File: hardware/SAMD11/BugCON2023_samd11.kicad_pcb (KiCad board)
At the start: 2 copper layers, 47.9 x 38.3 mm, 26 parts, among them J1 Conn_01x04_Pin, J2 Conn_01x04_Pin, P1 USB_C_Plug_USB2.0, Q1 DMG3415U-7, SW1 SW_Push, SW2 ON, U1 ATSAMD11C14A-SS, U2 AP2112K-3.3

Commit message: add pins of usb on samd11
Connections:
- U1 pad 10: unconnected-(U1-PA25-Pad10) -> /D+
- U1 pad 9: unconnected-(U1-PA24-Pad9) -> /D-
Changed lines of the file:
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@@
   (net 28 "unconnected-(U1-PA08{slash}XIN-Pad2)")
   (net 29 "unconnected-(U1-PA09{slash}XOUT-Pad3)")
-  (net 30 "unconnected-(U1-PA24-Pad9)")
-  (net 31 "unconnected-(U1-PA25-Pad10)")
-  (net 32 "unconnected-(U1-PA04-Pad14)")
+  (net 30 "unconnected-(U1-PA04-Pad14)")
   (footprint "BugCON2023_samd11:bug_silk_5" (layer "F.Cu")
     (at 166.61 95.66)
@@
       (net 21 "/SWDIO") (pinfunction "PA31/SWDIO") (pintype "bidirectional"))
     (pad "9" smd roundrect (at 2.475 -2.54 270) (size 1.95 0.6) (layers "B.Cu" "B.Paste" "B.Mask") (roundrect_rratio 0.25)
-      (net 30 "unconnected-(U1-PA24-Pad9)") (pinfunction "PA24") (pintype "bidirectional+no_connect"))
+      (net 15 "/D-") (pinfunction "PA24") (pintype "bidirectional"))
     (pad "10" smd roundrect (at 2.475 -1.27 270) (size 1.95 0.6) (layers "B.Cu" "B.Paste" "B.Mask") (roundrect_rratio 0.25)
-      (net 31 "unconnected-(U1-PA25-Pad10)") (pinfunction "PA25") (pintype "bidirectional+no_connect"))
+      (net 14 "/D+") (pinfunction "PA25") (pintype "bidirectional"))
     (pad "11" smd roundrect (at 2.475 0 270) (size 1.95 0.6) (layers "B.Cu" "B.Paste" "B.Mask") (roundrect_rratio 0.25)
       (net 2 "GND") (pinfunction "GND") (pintype "power_in"))
@@
       (net 22 "unconnected-(U1-PA02-Pad13)") (pinfunction "PA02") (pintype "bidirectional+no_connect"))
     (pad "14" smd roundrect (at 2.475 3.81 270) (size 1.95 0.6) (layers "B.Cu" "B.Paste" "B.Mask") (roundrect_rratio 0.25)
-      (net 32 "unconnected-(U1-PA04-Pad14)") (pinfunction "PA04") (pintype "bidirectional+no_connect"))
+      (net 30 "unconnected-(U1-PA04-Pad14)") (pinfunction "PA04") (pintype "bidirectional+no_connect"))
     (model "${KICAD6_3DMODEL_DIR}/Package_SO.3dshapes/SOIC-14_3.9x8.7mm_P1.27mm.wrl"
       (offset (xyz 0 0 0))

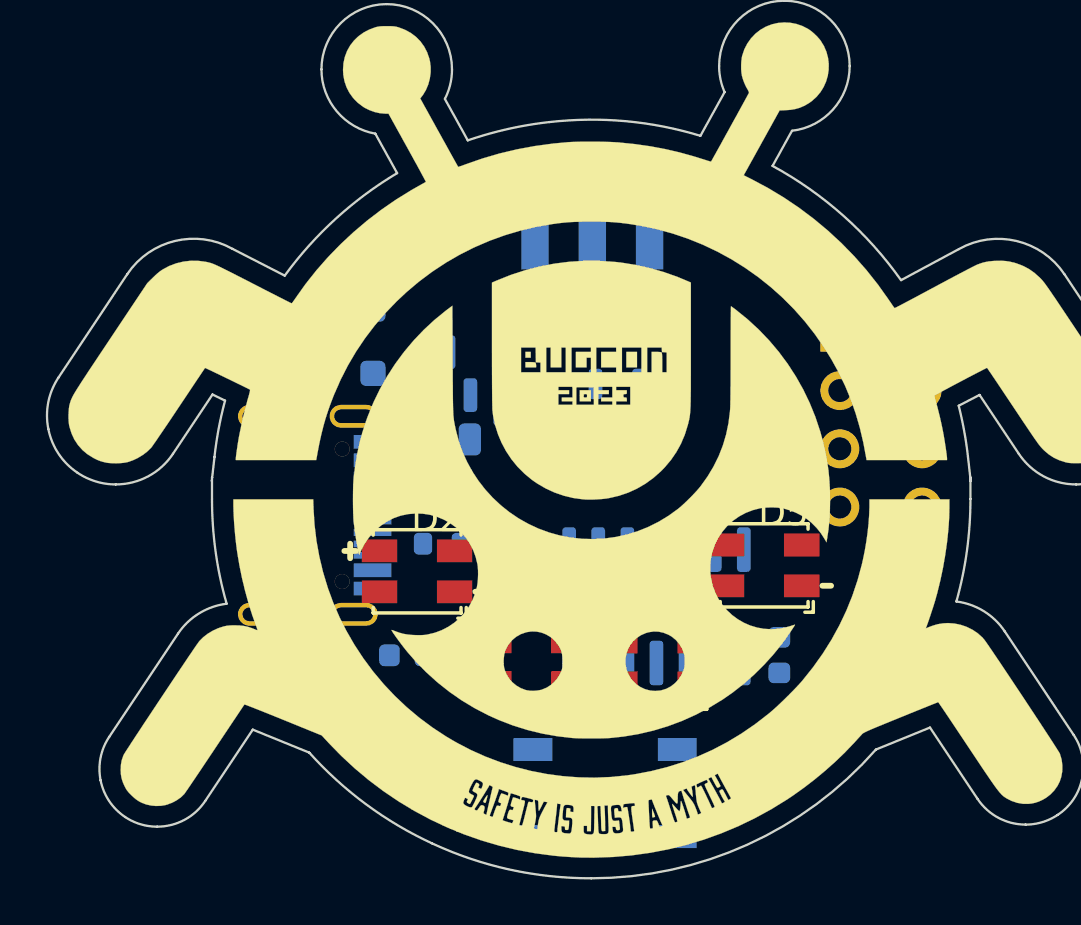
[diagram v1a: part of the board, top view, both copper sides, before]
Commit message: add floorplan to samd11
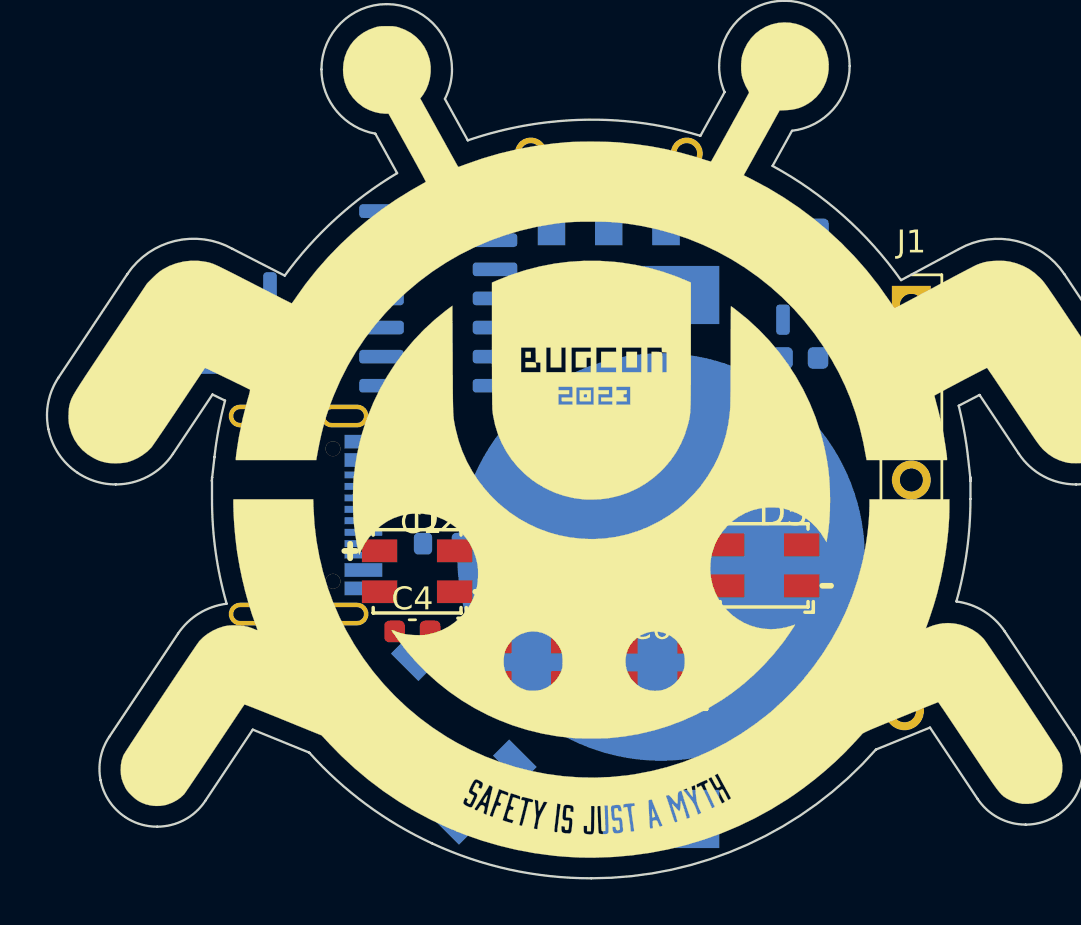
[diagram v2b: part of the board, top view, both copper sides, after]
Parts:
- added BT1: Battery_Cell, BugCON2023_samd11:BATHLD001THM, B.Cu at (143.2, 70.3)
- C1, C4, C6, C7, J1: moved to F.Cu
- moved U1 16.5 mm to (133.5, 59.1), turned to 180 degrees
- moved C1 13.6 mm to (132.7, 67.4), turned to 180 degrees
- moved R2 12.8 mm to (121.9, 62.2), turned to -90 degrees
- moved F1 11.2 mm to (123.6, 60.9), turned to 90 degrees
- moved R3 11.0 mm to (126.2, 62.4), turned to 180 degrees
- moved D1 11.0 mm to (119.9, 63.3)
- moved R4 10.6 mm to (138.4, 59.5), turned to -90 degrees
- moved C5 9.76 mm to (127.3, 75.5)
- moved J2 8.92 mm to (153.8, 69.4)
- moved C2 8.65 mm to (149.3, 56.0)
- moved U2 8.65 mm to (149.5, 58.9)
- moved C3 8.65 mm to (149.3, 61.7)
- moved Q1 8.26 mm to (126.1, 59.6)
- moved SW1 7.85 mm to (133.2, 78.4), turned to -45 degrees
- moved C6 6.18 mm to (142.7, 72.0), turned to 180 degrees
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
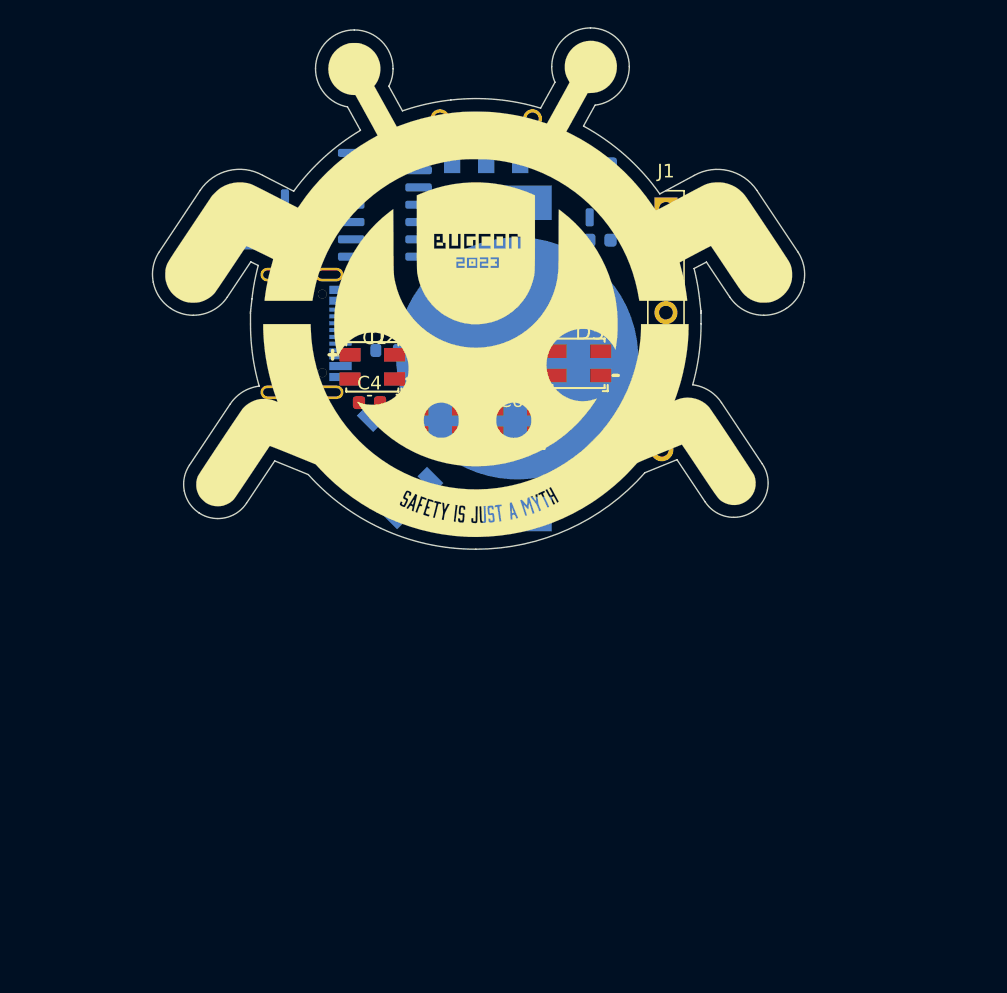
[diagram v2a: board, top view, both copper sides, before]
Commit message: upd floorplan on samd11
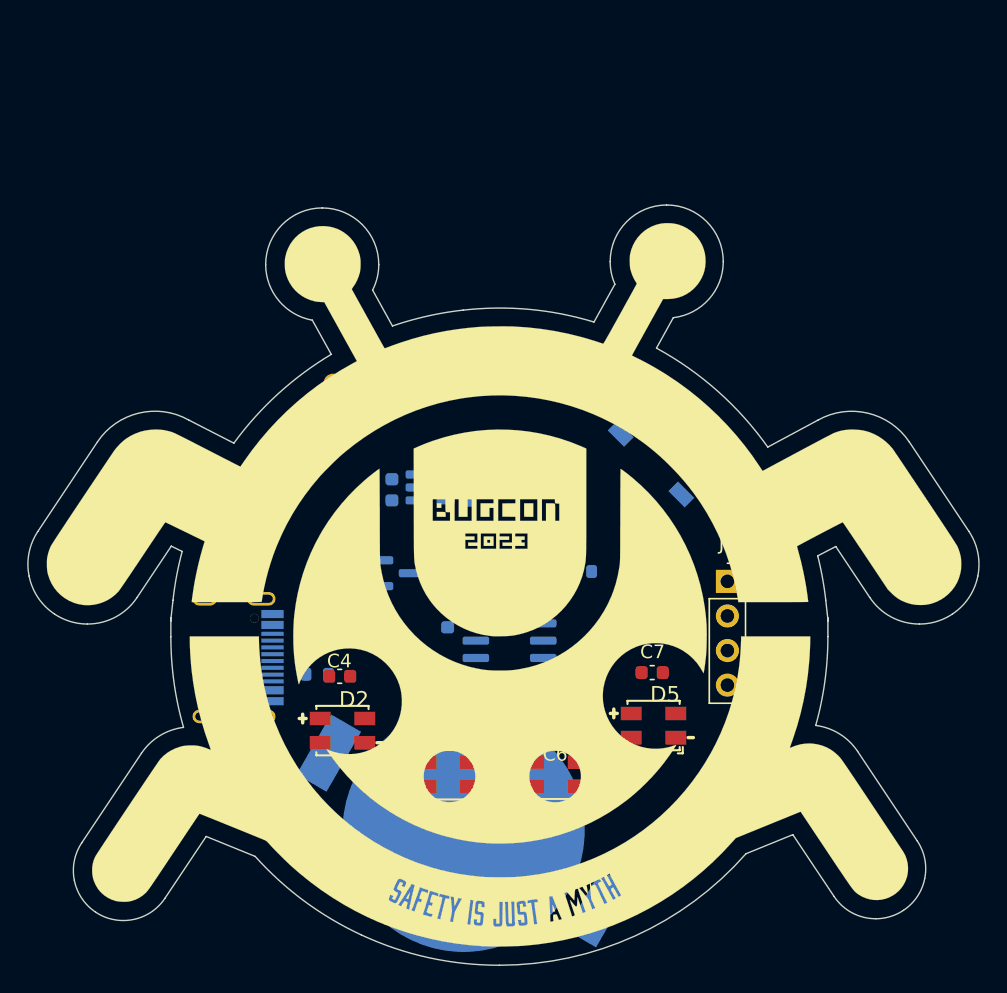
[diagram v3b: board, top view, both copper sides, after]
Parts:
- removed the Ref** at (166.6, 95.7)
- added ?: , , F.Cu at (141.8, 75.2)
- added Ref**: Val**, BugCON2023_samd11:bug-Silk_7, F.Cu at (142.2, 87.0)
- C1: moved to B.Cu
- C5: moved to F.Cu
- moved BT1 34.9 mm to (139.2, 105.0), turned to 150 degrees
- moved U1 32.1 mm to (142.6, 89.8)
- moved R2 29.2 mm to (128.6, 90.6), turned to 180 degrees
- moved F1 28.5 mm to (128.8, 88.9), turned to 0 degrees
- moved C2 28.4 mm to (134.0, 80.0), turned to 90 degrees
- moved R4 28.1 mm to (147.8, 86.0), turned to 0 degrees
- moved Q1 27.8 mm to (134.3, 86.1), turned to 0 degrees
- moved J1 27.7 mm to (158.6, 86.7)
- moved D5 27.2 mm to (153.2, 97.3)
- moved C7 27.0 mm to (153.1, 93.4), turned to 180 degrees
- moved D2 26.8 mm to (130.4, 97.7)
- moved J2 26.3 mm to (162.3, 94.3)
- moved C6 26.2 mm to (146.0, 98.0)
- moved D4 26.1 mm to (146.0, 100.9)
- moved D3 26.0 mm to (138.1, 100.9)
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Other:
- board size 47.9 x 38.3 mm -> 69.8 x 55.8 mm

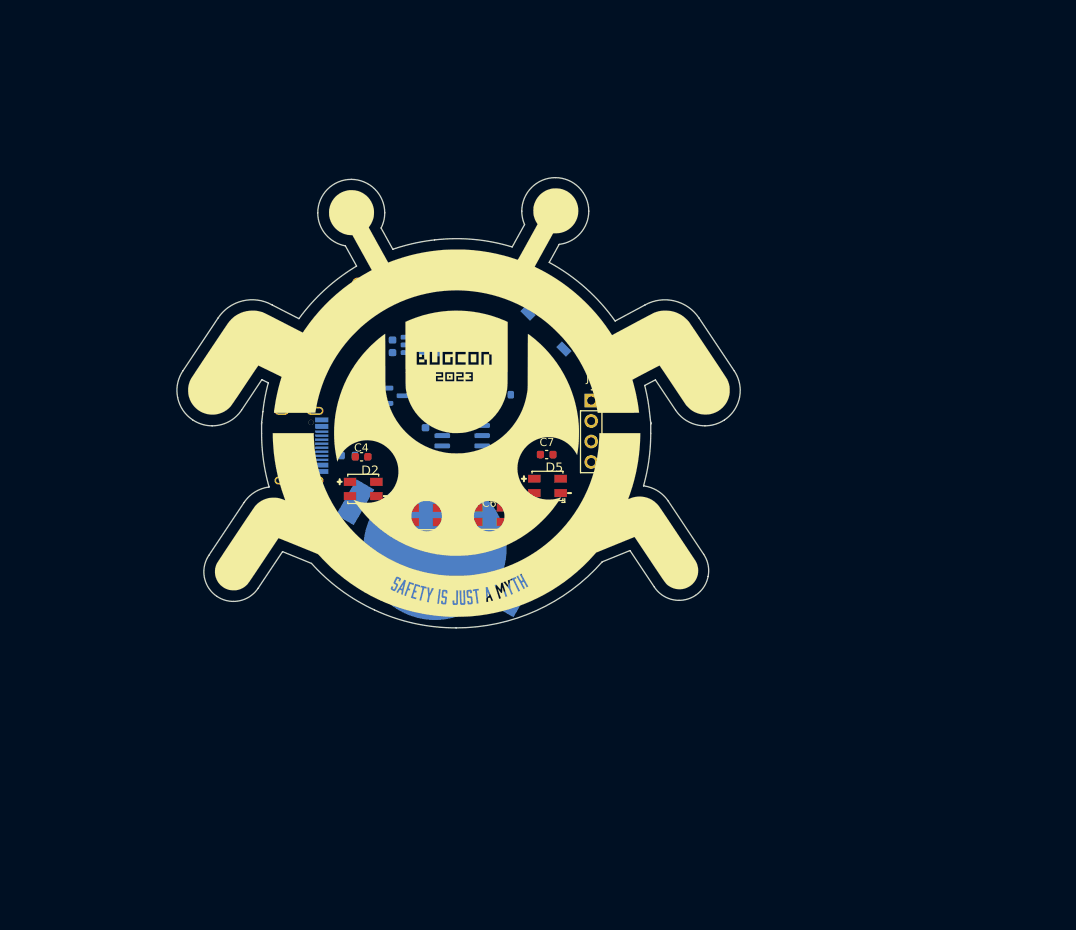
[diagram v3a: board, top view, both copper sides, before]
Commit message: upd BOM on Samd11 badge
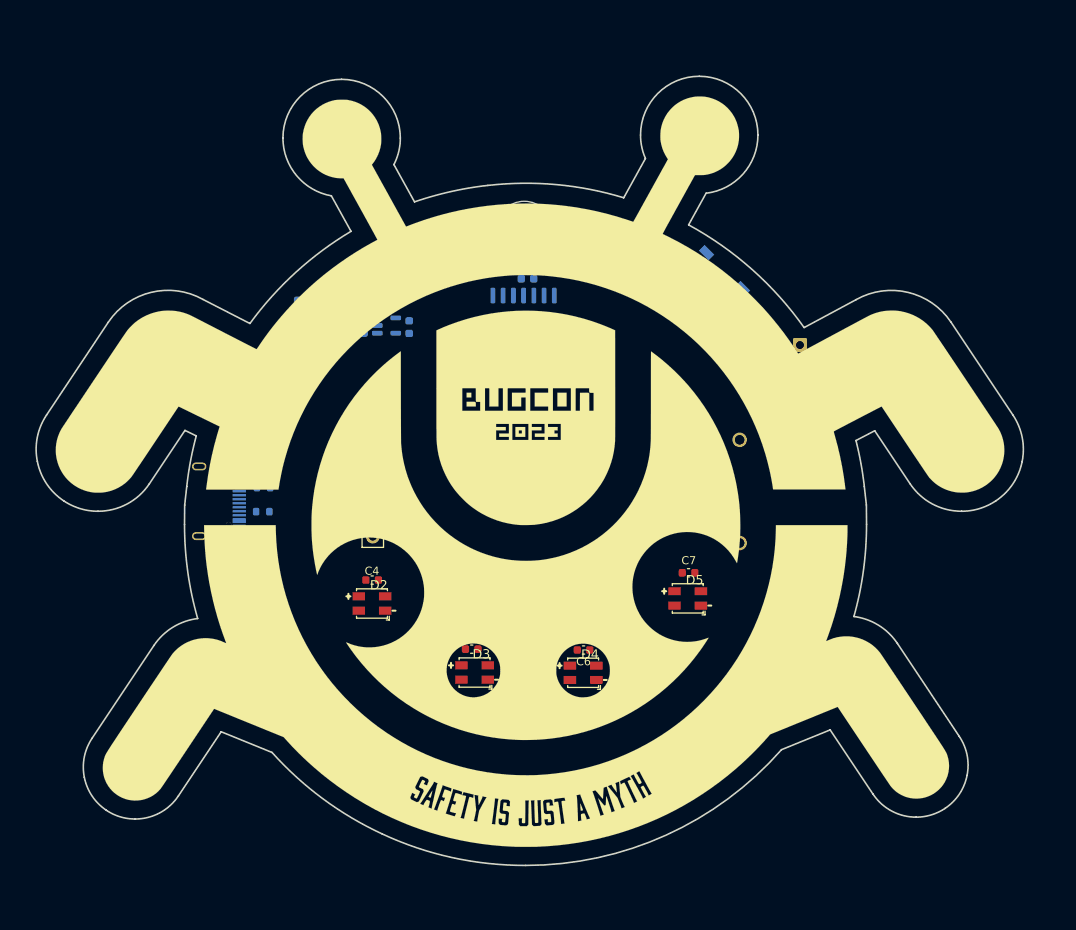
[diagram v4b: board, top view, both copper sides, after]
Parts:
- removed the Ref** at (142.2, 87.0)
- added Ref**: Val**, BugCON2023_samd11:Bugcon_svg, F.Cu at (151.0, 95.5)
- BT1: footprint BugCON2023_samd11:BATHLD001THM -> BugCON2023_samd11:BAT_12BH331P-GR
- SW2: footprint BugCON2023_samd11:JS102011SAQN -> BugCON2023_samd11:SW-TH_SK12D07VG4
- moved J1 28.6 mm to (131.5, 96.0)
- moved J2 26.5 mm to (184.5, 79.8)
- moved C7 22.9 mm to (170.7, 108.1)
- moved C6 22.9 mm to (157.7, 117.7)
- moved D4 22.8 mm to (157.6, 120.5)
- moved D5 22.3 mm to (170.6, 111.3)
- moved C1 21.8 mm to (150.7, 71.6), turned to 180 degrees
- moved C5 20.5 mm to (143.8, 117.5)
- moved D3 20.4 mm to (144.2, 120.5)
- moved SW1 20.0 mm to (173.8, 71.9), turned to -45 degrees
- moved U1 15.6 mm to (150.2, 76.2), turned to 90 degrees
- moved SW2 15.4 mm to (129.9, 60.4), turned to 120 degrees
- moved C4 15.3 mm to (131.5, 109.0)
- moved D2 14.3 mm to (131.4, 111.9)
- moved ? 13.0 mm to (150.3, 65.5)
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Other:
- board size 69.8 x 55.8 mm -> 122.4 x 97.9 mm

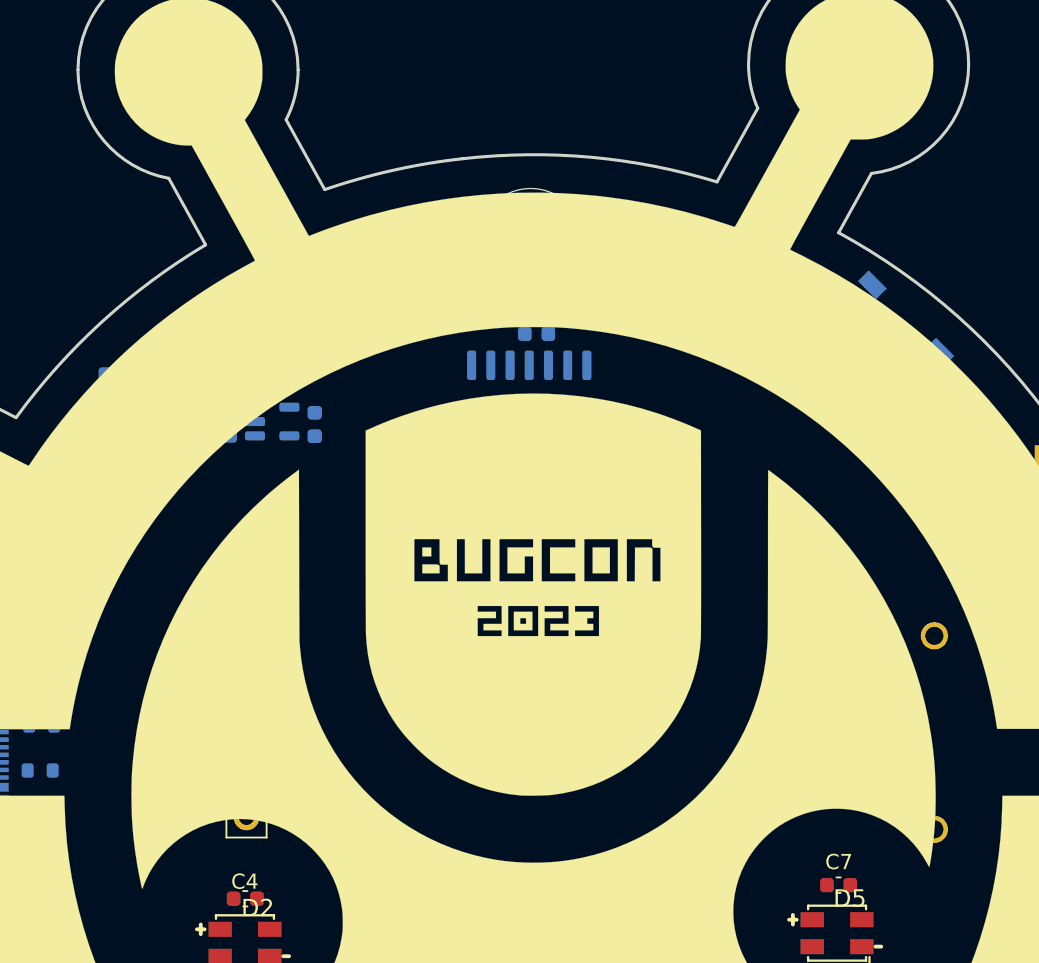
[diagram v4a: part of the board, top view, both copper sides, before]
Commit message: change battery connector
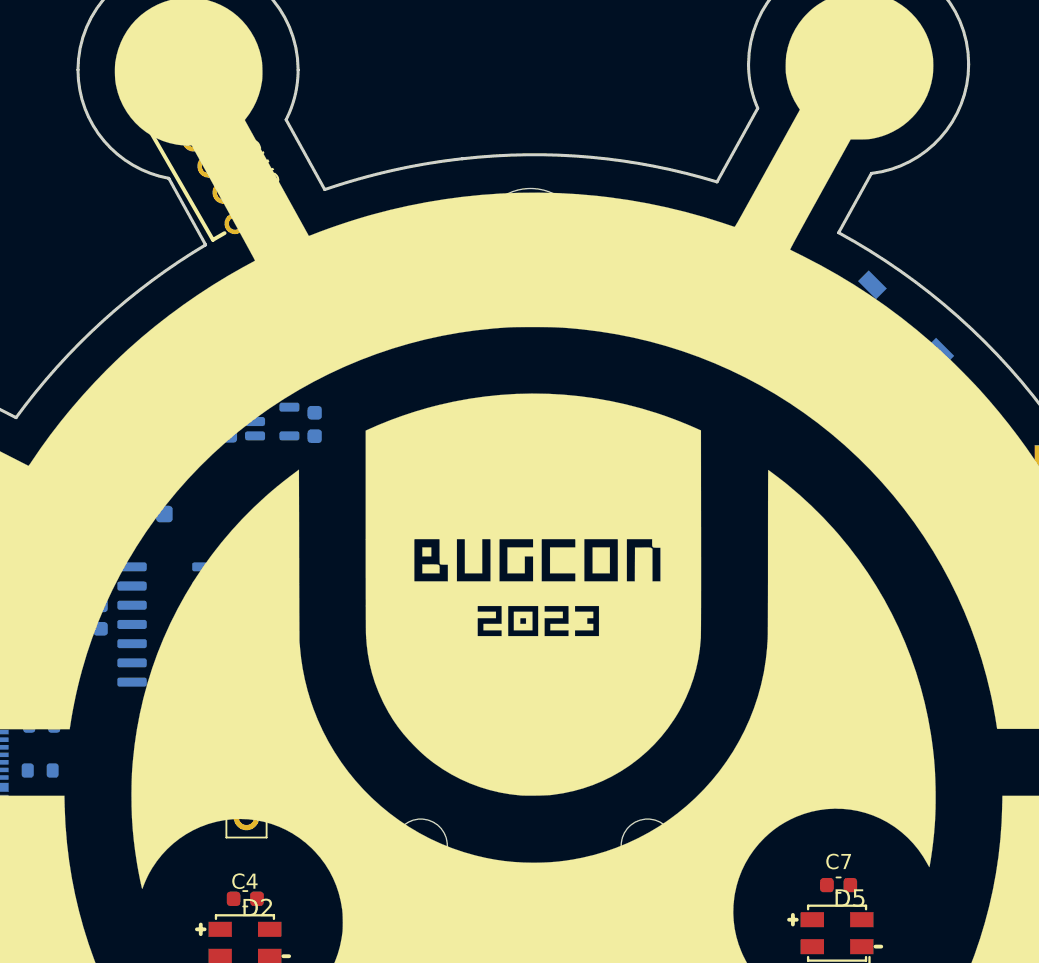
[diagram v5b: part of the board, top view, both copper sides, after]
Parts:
- BT1: footprint BugCON2023_samd11:BAT_12BH331P-GR -> BugCON2023_samd11:BAT_2462
- SW2: moved to F.Cu
- moved C1 34.4 mm to (121.9, 90.4), turned to -90 degrees
- moved U1 28.0 mm to (126.4, 90.8), turned to 180 degrees
- moved D1 7.41 mm to (126.1, 82.1), turned to 90 degrees
- moved Q1 7.26 mm to (122.9, 82.3), turned to 180 degrees
- moved R3 3.60 mm to (123.0, 79.7), turned to 180 degrees
- moved BT1 1.16 mm to (150.6, 105.5), turned to 90 degrees
- moved SW2 0.83 mm to (129.1, 60.5), turned to -60 degrees
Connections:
- C1 pad 1: +3V3 -> +3.3V
- C2 pad 1: Net-(SW2-B) -> VBUS
- D1 pad 2: VBUS -> +3V3
- J1 pad 3: +3V3 -> +3.3V
- Q1 pad 1: VBUS -> +3V3
- R3 pad 1: VBUS -> +3V3
- SW1 pad 1: +3V3 -> +3.3V
- SW2 pad 2: Net-(SW2-B) -> +3.3V
- U1 pad 12: +3V3 -> +3.3V
- U2 pad 1: Net-(SW2-B) -> VBUS
- U2 pad 3: Net-(SW2-B) -> VBUS
